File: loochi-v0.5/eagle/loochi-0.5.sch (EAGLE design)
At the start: 49 parts, among them IC1 ATTINY61M, J1 SPI_PRG, J2 POWER_JACKSMD, Q1 PMN25ENSOT457, Q2 PMN25ENSOT457, Q3 PMN25ENSOT457, Q4 FDC654P, U1 LZ4-00MC00BIGPADS, U2 APDS-9007, X1 SMA-SMD

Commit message: loochi-0.5.brd
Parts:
- removed F1: MPZ2012, rcl:R-EU_R0603
- removed J3: (no value), con-lstb:MA05-2
- added BLUE: (no value), WCI:500003
- added C14, C16: 100n, rcl:C-EUC0603
- added C19: 0.1uF, rcl:C-EUC0603K
- added F2: MPZ2012, rcl:R-EU_R0603
- added P1: 53047-0610, con-molex-picoblade:53047-0610
- added R18: 2, rcl:R-EU_R0603
- added R4: 1k, rcl:R-EU_R0603
- C7: value 10uF X5R Low ESR -> 10u
- Q4: value FDC654P -> SI7617DN; device mosfet:FDC654P -> Oma:SI7617DN
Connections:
- removed net N$6: F1.1, Q4.S
- removed net RSTB: J3.5, U$2.SPI_CSB
- new net N$12: BLUE.C, R4.2
- new net N$16: R4.1, U$2.LED(1)
- new net N$21: C12.+, R18.1
- new net N$22: C19.2, F2.2, U$1.ON/!OFF!, U$1.VIN
- new net SPI_CSB: P1.3, U$2.SPI_CSB
- new net SPI_RESET: P1.1, U$2.SPI_RESET
- net GND: now also C16.2, C19.1, P1.6, Q4.4; no longer J3.10, J3.6, J3.8, Q4.G
- net N$10: now also Q4.5, Q4.6, Q4.7, Q4.8; no longer Q4.D
- net N$15: now also C14.2, C16.1, X1G$1.1; no longer J3.3, U$2.SPI_RESET
- net N$2: now also C14.1; no longer X1G$1.1
- net SPI_CLK: now also P1.4; no longer J3.7
- net SPI_MISO: now also P1.5; no longer J3.9
- net SPI_MOSI: now also P1.2; no longer J3.1
- net V+: now also F2.1, Q4.1, Q4.2, Q4.3, R18.2; no longer C12.+, F1.2, U$1.ON/!OFF!, U$1.VIN
- net VCC: now also BLUE.A; no longer J3.2, J3.4
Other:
- note added: "PIO(6)"
- moved on the sheet: C12, C7, C9, J2, U$1

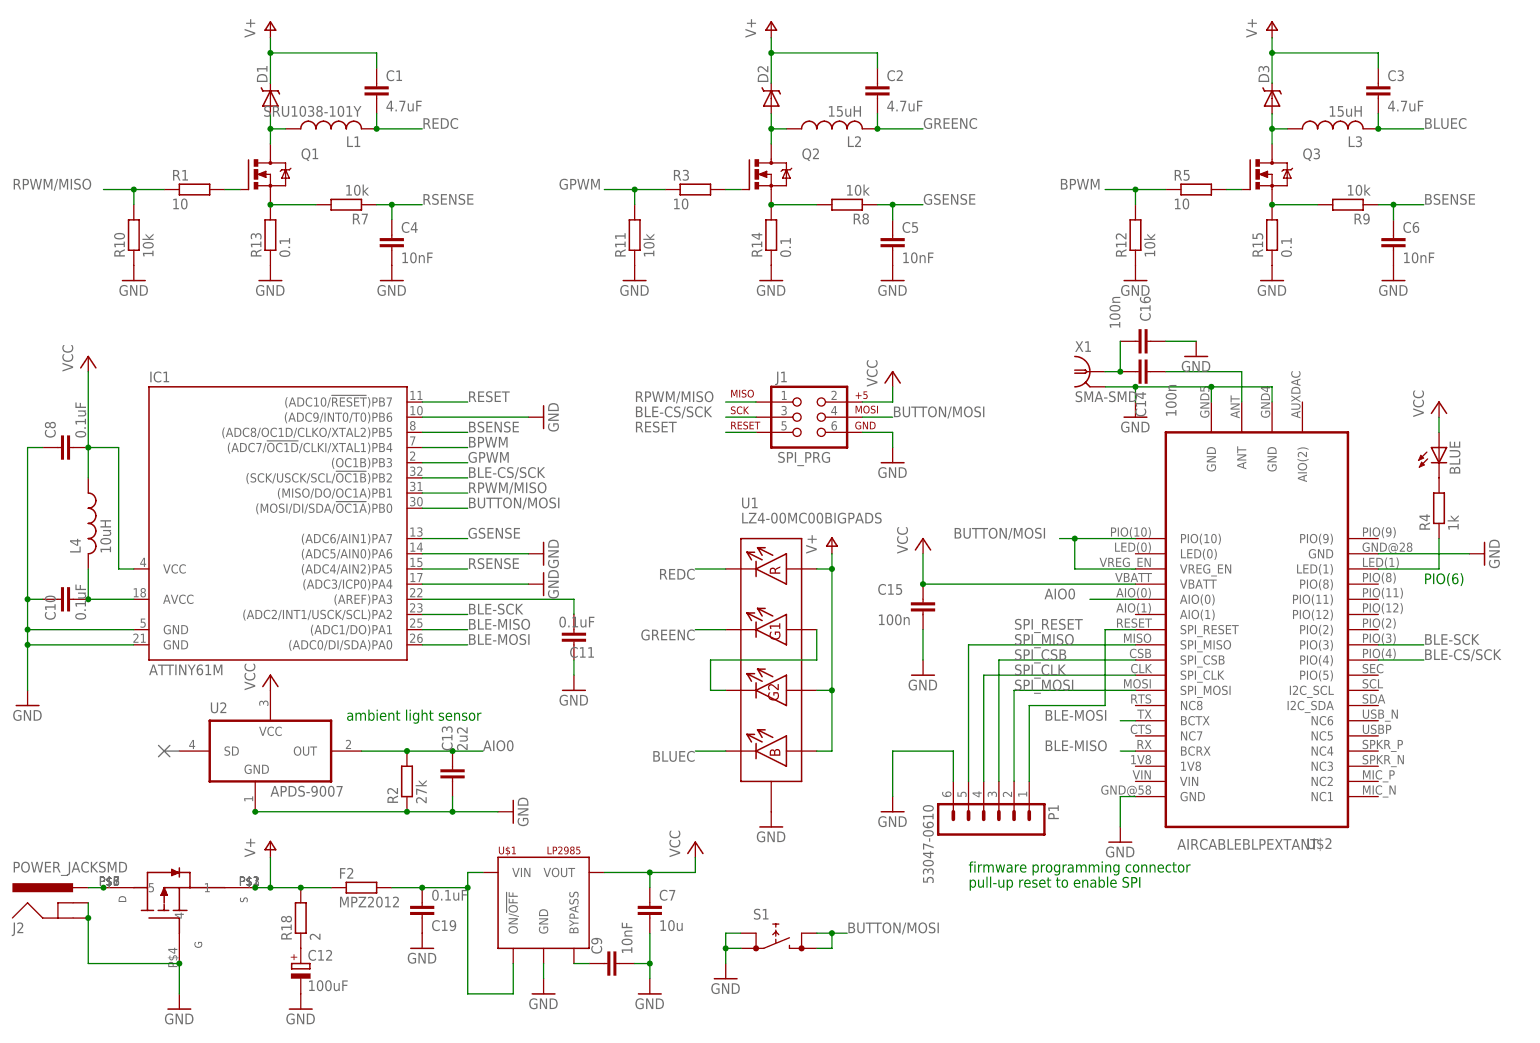
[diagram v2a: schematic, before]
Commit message: More work on the board - almost final (antenna trace needs rework)
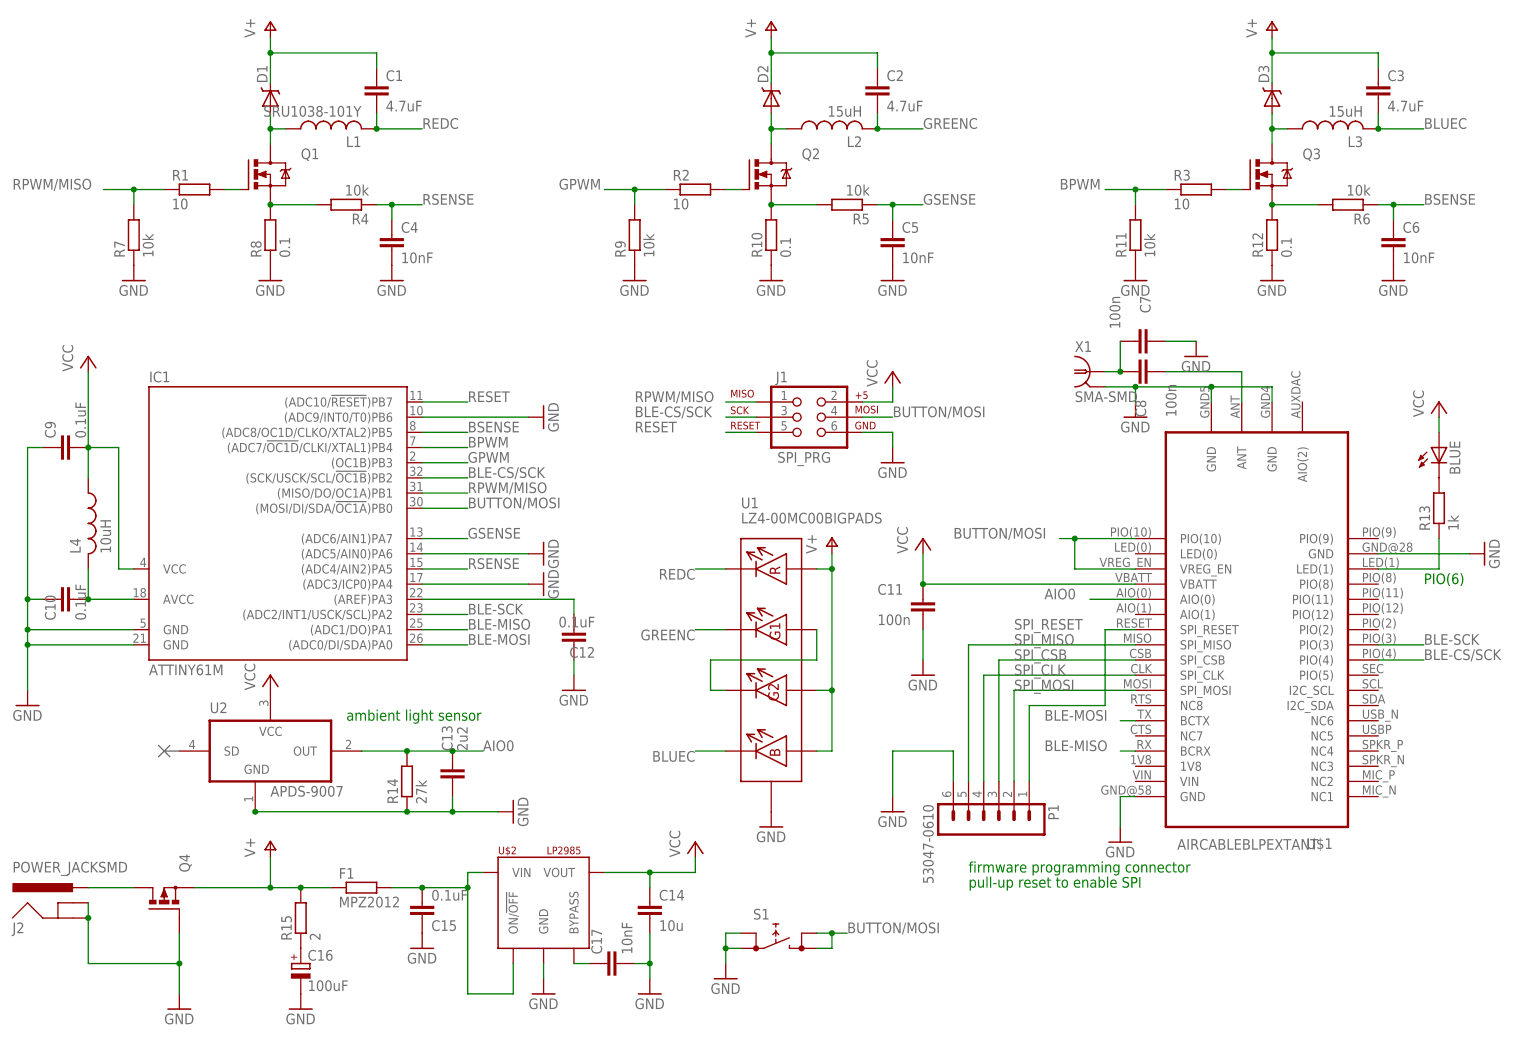
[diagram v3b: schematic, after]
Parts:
- removed C19: 0.1uF, rcl:C-EUC0603K
- removed R18: 2, rcl:R-EU_R0603
- added C17: 10nF, rcl:C-EUC0603
- added R6: 10k, rcl:R-EU_R0603
- C1, C2, C3: device rcl:C-EUC0805 -> rcl:C-EUC0603
- C11, C8: value 0.1uF -> 100n; PARTNO (none) -> *
- C12: value 100uF -> 0.1uF; device rcl:CPOL-EUD -> rcl:C-EUC0603
- C14: value 100n -> 10u; PARTNO * -> (none)
- C15: value 100n -> 0.1uF; device rcl:C-EUC0603 -> rcl:C-EUC0603K; PARTNO * -> (none)
- C16: value 100n -> 100uF; device rcl:C-EUC0603 -> rcl:CPOL-EUD; PARTNO * -> (none)
- C7: value 10u -> 100n; PARTNO (none) -> *
- C9: value 10nF -> 0.1uF
- Q4: value SI7617DN -> (none); device Oma:SI7617DN -> mosfet:FDC654P
- R10, R12, R8: value 10k -> 0.1
- R13: value 0.1 -> 1k
- R14: value 0.1 -> 27k
- R15: value 0.1 -> 2
- R2: value 27k -> 10
- R4: value 1k -> 10k
- R5: value 10 -> 10k
- U$1: value LP2985 -> AIRCABLEBLPEXTANT; device ti-regulators:LP2985 -> aircable:AIRCABLEBLPEXTANT
- U$2: value AIRCABLEBLPEXTANT -> LP2985; device aircable:AIRCABLEBLPEXTANT -> ti-regulators:LP2985
- renumbered F2 to F1
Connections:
- net AIO0: now also R14.2, U$1.AIO(0); no longer R2.2, U$2.AIO(0)
- net BLE-CS/SCK: now also U$1.PIO(4); no longer U$2.PIO(4)
- net BLE-MISO: now also U$1.BCRX; no longer U$2.BCRX
- net BLE-MOSI: now also U$1.BCTX; no longer U$2.BCTX
- net BLE-SCK: now also U$1.PIO(3); no longer U$2.PIO(3)
- net BPWM: now also R11.2, R3.1; no longer R12.2, R5.1
- net BSENSE: now also R6.1; no longer R9.1
- net BUTTON/MOSI: now also U$1.PIO(10), U$1.VREG_EN; no longer U$2.PIO(10), U$2.VREG_EN
- net GND: now also C12.1, C14.2, C16.-, C17.2, C9.1, Q4.G, R7.1, R8.1, R9.1, U$1.GND@28, U$1.GND@32, U$1.GND@34, U$1.GND@58, U$2.GND; no longer C12.-, C16.2, C19.1, C8.1, C9.2, Q4.4, R13.1, R15.1, R2.1, U$1.GND, U$2.GND@28, U$2.GND@32, U$2.GND@34, U$2.GND@58
- net GPWM: now also R2.1, R9.2; no longer R11.2, R3.1
- net GSENSE: now also R5.1; no longer R8.1
- net N$10: now also Q4.D; no longer Q4.5, Q4.6, Q4.7, Q4.8
- net N$12: now also R13.2; no longer R4.2
- net N$13: now also C17.1, U$2.BYPASS; no longer C9.1, U$1.BYPASS
- net N$15: now also C7.1, C8.2; no longer C14.2, C16.1
- net N$16: now also R13.1, U$1.LED(1); no longer R4.1, U$2.LED(1)
- net N$17: now also R10.2, R5.2; no longer R14.2, R8.2
- net N$2: now also C8.1, U$1.ANT; no longer C14.1, U$2.ANT
- net N$21: now also C16.+, R15.1; no longer C12.+, R18.1
- net N$22: now also C15.2, U$2.ON/!OFF!, U$2.VIN; no longer C19.2, U$1.ON/!OFF!, U$1.VIN
- net N$25: now also R12.2, R6.2; no longer R15.2, R9.2
- net N$3: now also R3.2; no longer R5.2
- net N$4: now also R2.2; no longer R3.2
- net N$7: now also R4.2, R8.2; no longer R13.2, R7.2
- net N$9: now also C12.2; no longer C11.2
- net RPWM/MISO: now also R7.2; no longer R10.2
- net RSENSE: now also R4.1; no longer R7.1
- net SPI_CLK: now also U$1.SPI_CLK; no longer U$2.SPI_CLK
- net SPI_CSB: now also U$1.SPI_CSB; no longer U$2.SPI_CSB
- net SPI_MISO: now also U$1.SPI_MISO; no longer U$2.SPI_MISO
- net SPI_MOSI: now also U$1.SPI_MOSI; no longer U$2.SPI_MOSI
- net SPI_RESET: now also U$1.SPI_RESET; no longer U$2.SPI_RESET
- net V+: now also Q4.S, R15.2; no longer Q4.1, Q4.2, Q4.3, R18.2
- net VCC: now also C11.2, C14.1, C9.2, U$1.VBATT, U$2.VOUT; no longer C15.2, C7.1, C8.2, U$1.VOUT, U$2.VBATT
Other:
- moved on the sheet: C11, C14, C15, C7, C8, C9, R10, R11, R12, R13, R14, R15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
